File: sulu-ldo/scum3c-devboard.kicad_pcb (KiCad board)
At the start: 2 copper layers, 41.7 x 36.1 mm, 53 parts, among them J1 Conn_02x11_Odd_Even, J10 through_hole, J11 through_hole, J12 through_hole, J13 through_hole, J14 through_hole, J15 through_hole, J16 through_hole, J17 through_hole, J18 through_hole, J19 through_hole, J2 Conn_02x10_Odd_Even, J20 through_hole, J21 through_hole, J3 Conn_02x05_Odd_Even, J4 Conn_01x01_Male, J5 through_hole, J6 through_hole, J7 through_hole, J8 through_hole, J9 through_hole, U1 scum3, U2 LP5907MFX-1.8, U3 TLV70311DBVR, U9AB1 ICM-20948

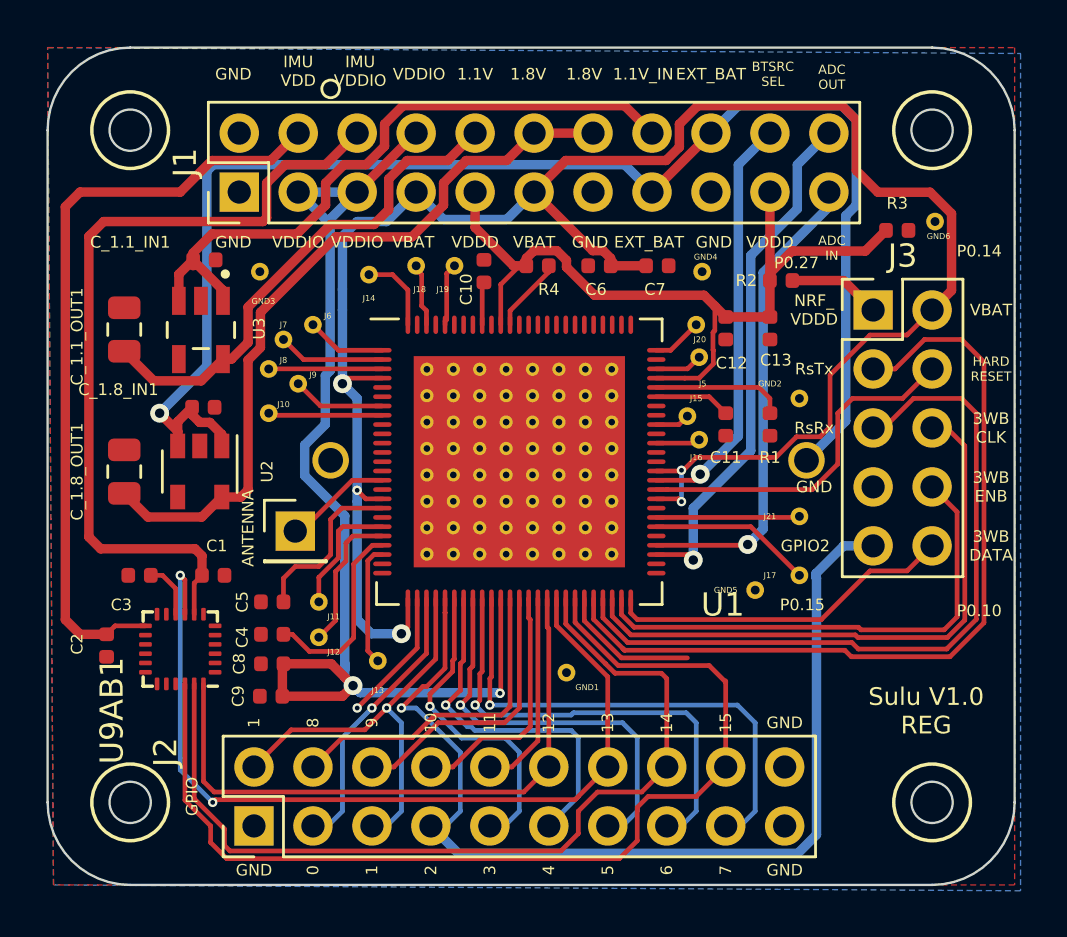
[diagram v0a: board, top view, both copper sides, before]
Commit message: added ldos
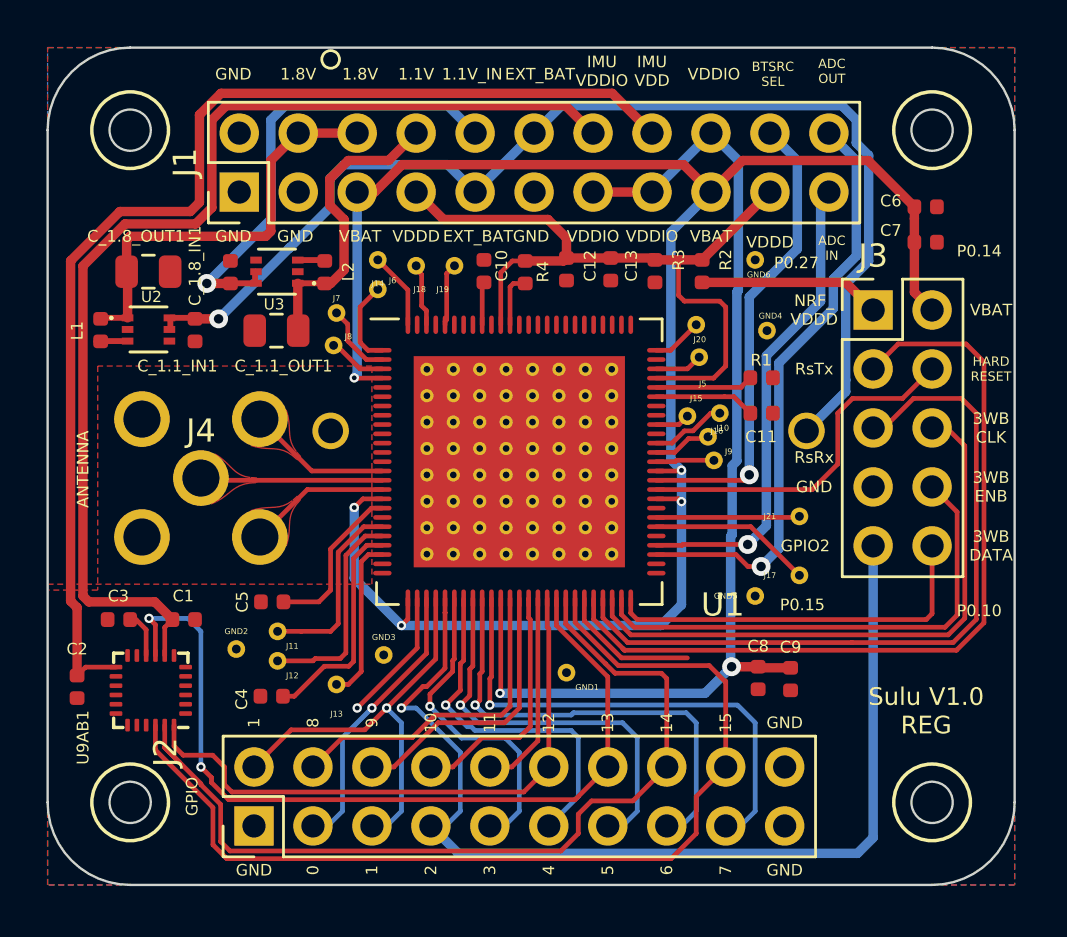
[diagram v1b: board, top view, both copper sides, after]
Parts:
- added L1: 2.2 uH, Inductor_SMD:L_0402_1005Metric, F.Cu at (108.3, 84.7)
- added L2: 2.2 uH, Inductor_SMD:L_0402_1005Metric, F.Cu at (118.0, 82.2)
- J4: value Conn_01x01_Male -> 73391-0060; footprint Connector_PinHeader_2.54mm:PinHeader_1x01_P2.54mm_Vertical -> downloaded_libs:MOLEX_73391-0060
- U2: value LP5907MFX-1.8 -> S-85S1AB18-I6T1U; footprint Package_TO_SOT_SMD:SOT-23-5 -> downloaded_libs:SOFL50P180X50-6N
- U3: value TLV70311DBVR -> S-85S1AB11-I6T1U; footprint downloaded_libs:SOT95P280X145-5N -> downloaded_libs:SOFL50P180X50-6N
- moved GND2 26.6 mm to (114.2, 98.4)
- moved C9 22.4 mm to (138.0, 99.7), turned to 270 degrees
- moved C8 20.9 mm to (136.7, 99.7), turned to 270 degrees
- moved J10 19.0 mm to (134.5, 89.3)
- moved J9 18.2 mm to (134.7, 90.3)
- moved GND3 17.4 mm to (120.5, 98.7)
- moved C6 14.3 mm to (143.9, 79.4), turned to 0 degrees
- moved C7 11.6 mm to (143.9, 80.9)
- moved R3 10.6 mm to (132.2, 82.1), turned to 270 degrees
- moved C_1.8_OUT1 8.68 mm to (110.4, 82.2), turned to 180 degrees
- moved GND6 7.92 mm to (136.5, 81.7)
- moved C12 7.31 mm to (128.4, 82.1)
- moved C13 7.31 mm to (130.3, 82.1)
- moved C_1.1_OUT1 6.56 mm to (115.9, 84.7), turned to 0 degrees
- moved U2 6.50 mm to (110.4, 84.7), turned to 0 degrees
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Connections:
- net /ANTENNA renamed /scumsheet/ANTENNA
- J1 pad 10: +1.1V_REG -> /1.1V_IN
- J1 pad 11: +VBAT -> GND
- J1 pad 12: +1.8V_REG -> +EXT_BAT
- J1 pad 13: GND -> +VDDIO
- J1 pad 14: +1.8V_REG -> /IMU_VDDIO
- J1 pad 15: +EXT_BAT -> +VDDIO
- J1 pad 16: /1.1V_IN -> /IMU_VDD
- J1 pad 17: GND -> +VBAT
- J1 pad 18: +EXT_BAT -> +VDDIO
- J1 pad 3: +VDDIO -> GND
- J1 pad 4: /IMU_VDD -> +1.8V_REG
- J1 pad 5: +VDDIO -> +VBAT
- J1 pad 6: /IMU_VDDIO -> +1.8V_REG
- J1 pad 7: +VBAT -> +VDDD
- J1 pad 8: +VDDIO -> +1.1V_REG
- J1 pad 9: +VDDD -> +EXT_BAT
- U1 pad 63: (no net) -> Net-(J9-Pad1)
- U1 pad 64: (no net) -> Net-(J10-Pad1)
- U1 pad 7: Net-(J9-Pad1) -> (no net)
- U1 pad 8: Net-(J10-Pad1) -> (no net)
- U2 pad 1: +EXT_BAT -> +1.8V_REG
- U2 pad 3: +EXT_BAT -> Net-(L1-Pad2)
- U2 pad 4: (no net) -> GND
- U2 pad 5: +1.8V_REG -> +EXT_BAT
- U3 pad 1: /1.1V_IN -> +1.1V_REG
- U3 pad 3: /1.1V_IN -> Net-(L2-Pad2)
- U3 pad 4: (no net) -> GND
- U3 pad 5: +1.1V_REG -> /1.1V_IN
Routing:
- net /IMU_VDD: track 33.0 -> 50.8 mm
- net +1.8V_REG: track 32.2 -> 19.1 mm
- net +EXT_BAT: track 63.3 -> 50.4 mm
- net GND: track 11.8 -> 24.2 mm
- net /IMU_VDDIO: track 35.9 -> 47.7 mm
- net /1.1V_IN: track 28.9 -> 20.9 mm, vias 0 -> 1
- net +1.1V_REG: track 22.5 -> 15.3 mm
- net +VDDD: track 37.2 -> 33.0 mm
- net +VBAT: track 86.3 -> 82.4 mm
- net +NRF_VDDD: track 4.00 -> 7.86 mm
- net /scumsheet/ANTENNA: track 4.66 -> 7.86 mm
- net +VDDIO: track 50.0 -> 46.9 mm
- net /SENSOR_LDO_OUTPUT: track 22.5 -> 25.6 mm
- net Net-(J12-Pad1): track 6.24 -> 9.20 mm
- net Net-(J11-Pad1): track 5.37 -> 8.19 mm
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
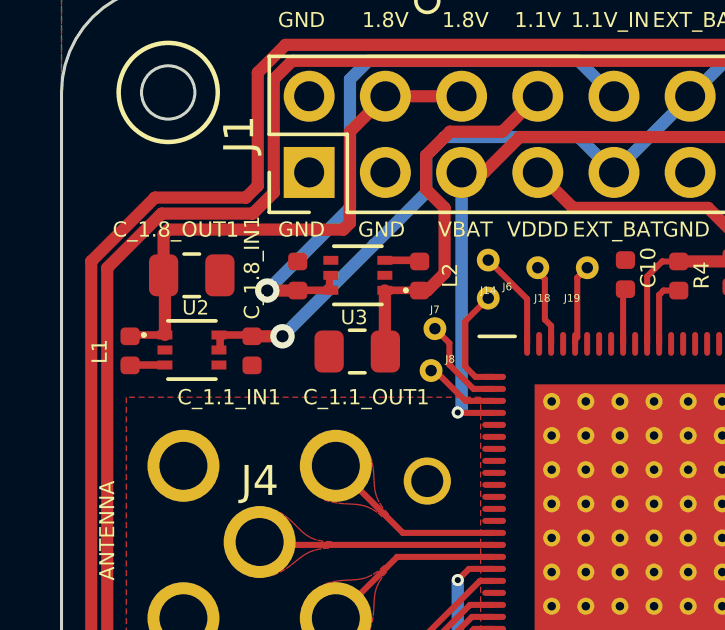
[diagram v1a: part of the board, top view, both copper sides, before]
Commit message: put ldos on pcb
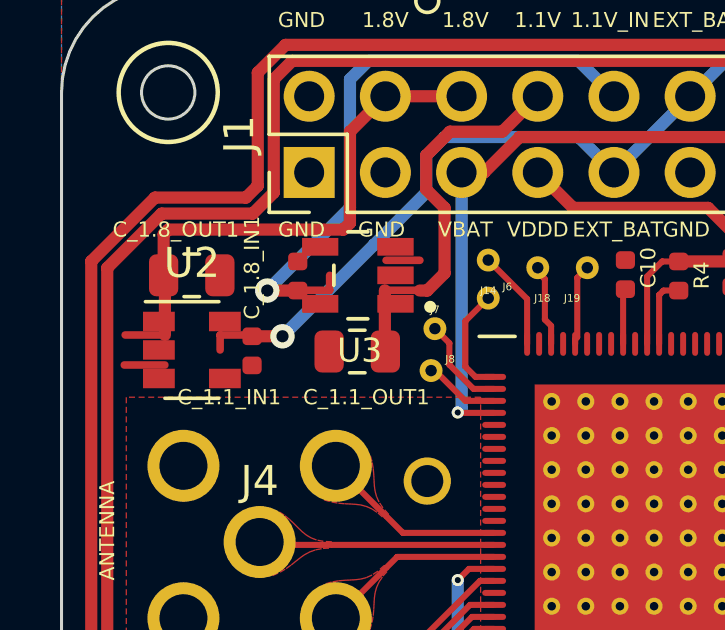
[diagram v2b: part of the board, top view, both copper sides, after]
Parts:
- removed L1, L2: 2.2 uH, Inductor_SMD:L_0402_1005Metric
- U2: value S-85S1AB18-I6T1U -> LP5907MFX-1.8; footprint downloaded_libs:SOFL50P180X50-6N -> Package_TO_SOT_SMD:SOT-23-5
- U3: value S-85S1AB11-I6T1U -> TLV70311DBVR; footprint downloaded_libs:SOFL50P180X50-6N -> downloaded_libs:SOT95P280X145-5N
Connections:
- U2 pad 1: +1.8V_REG -> +EXT_BAT
- U2 pad 3: Net-(L1-Pad2) -> +EXT_BAT
- U2 pad 4: GND -> (no net)
- U2 pad 5: +EXT_BAT -> +1.8V_REG
- U3 pad 1: +1.1V_REG -> /1.1V_IN
- U3 pad 3: Net-(L2-Pad2) -> /1.1V_IN
- U3 pad 4: GND -> (no net)
- U3 pad 5: /1.1V_IN -> +1.1V_REG

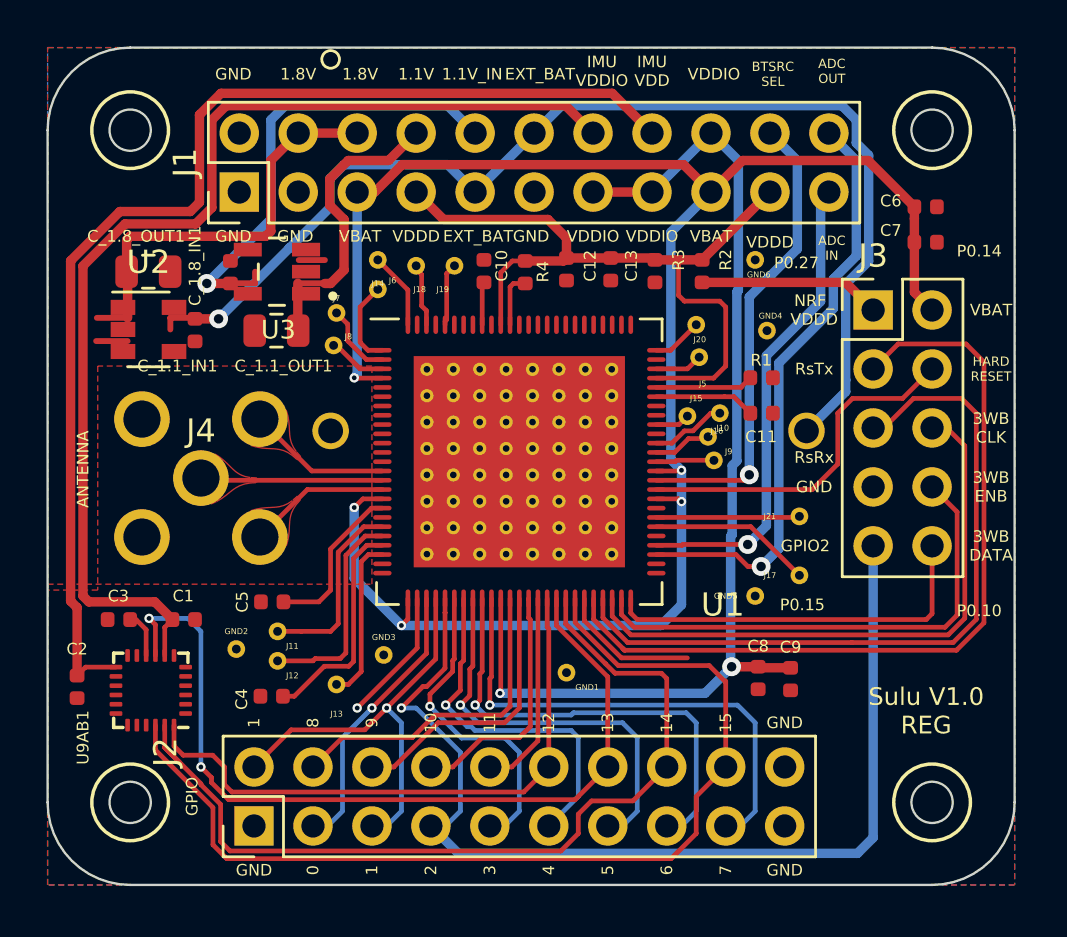
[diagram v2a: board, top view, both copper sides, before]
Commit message: moved labels for LDOOs
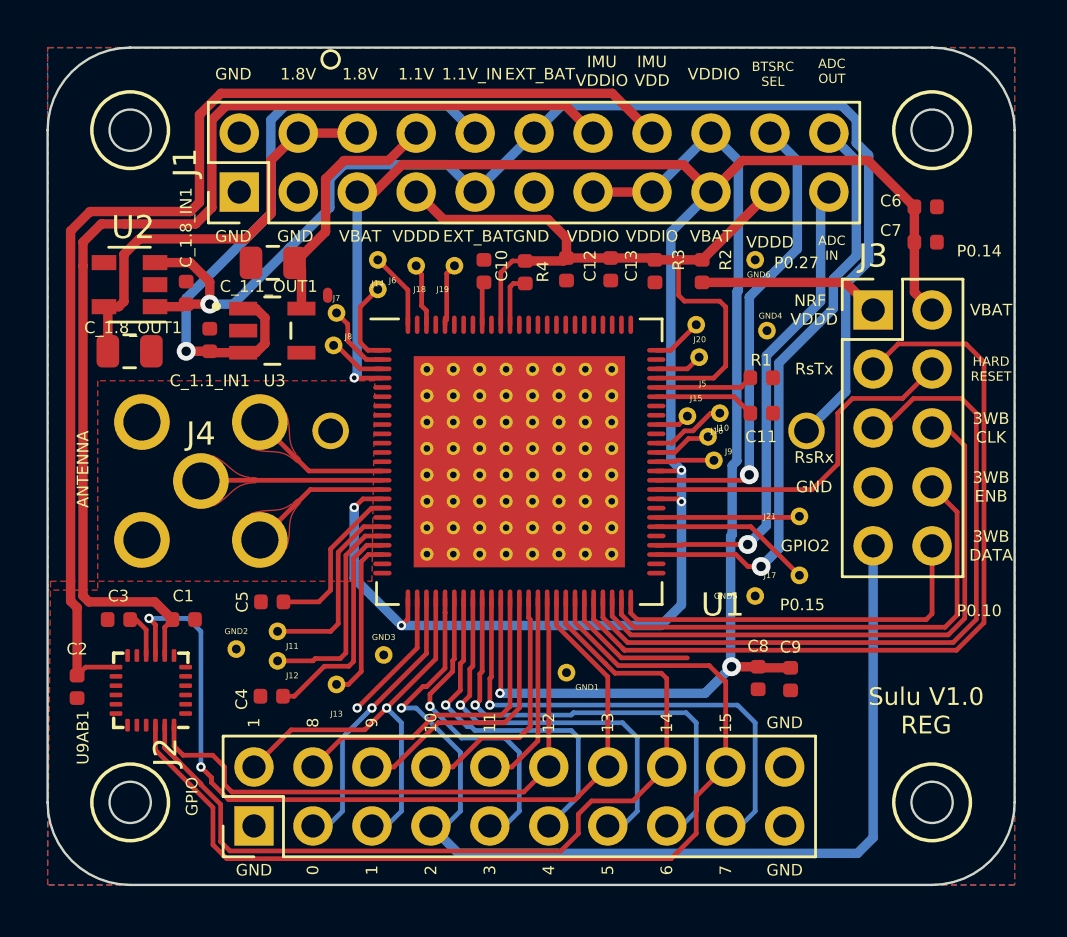
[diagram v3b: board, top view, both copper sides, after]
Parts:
- moved C_1.8_OUT1 3.52 mm to (109.6, 85.6)
- moved C_1.1_IN1 3.05 mm to (113.0, 85.1)
- moved C_1.1_OUT1 2.93 mm to (115.7, 81.8)
- moved U3 2.55 mm to (115.7, 84.7), turned to 0 degrees
- moved U2 2.10 mm to (109.6, 82.7), turned to 180 degrees
- moved C_1.8_IN1 1.65 mm to (112.0, 83.1), turned to 90 degrees
- moved J4 0.13 mm to (112.6, 91.2)
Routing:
- net /1.1V_IN: track 20.9 -> 27.6 mm
- net +1.1V_REG: track 15.3 -> 11.0 mm
- net +EXT_BAT: track 50.4 -> 54.1 mm
- net Net-(L1-Pad2): track 1.36 -> 0.00 mm
- net Net-(L2-Pad2): track 1.13 -> 0.00 mm
- net /IMU_VDD: track 50.8 -> 51.5 mm
- net /IMU_VDDIO: track 47.7 -> 48.3 mm
